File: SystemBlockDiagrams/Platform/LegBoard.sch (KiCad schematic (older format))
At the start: 12 parts

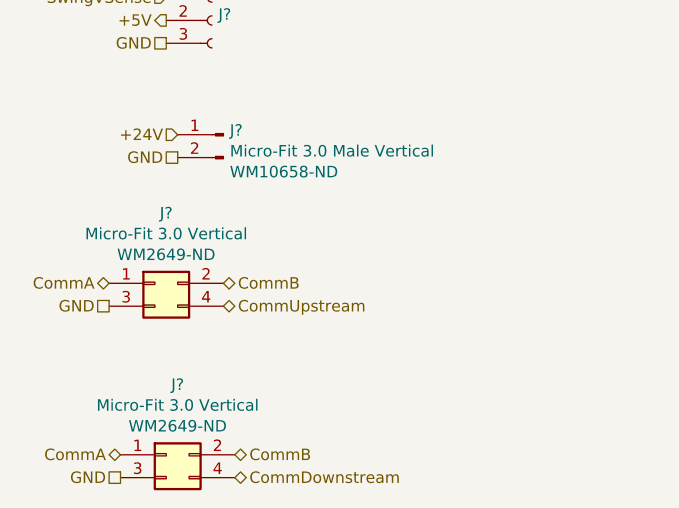
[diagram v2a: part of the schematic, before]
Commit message: Update to show all legs on block diagram
Add radios to platform diagram
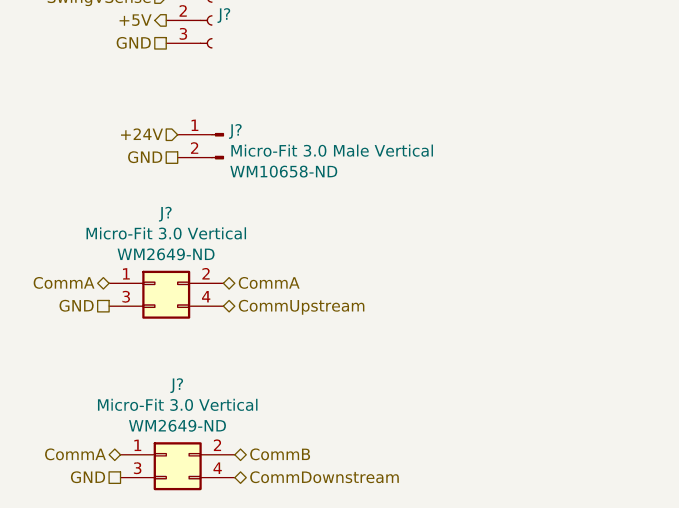
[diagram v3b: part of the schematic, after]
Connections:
- net CommA: now also J?.2 (Pin_2)
- net CommB: no longer J?.2 (Pin_2)
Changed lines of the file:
@@
 $Descr A4 11693 8268
 encoding utf-8
-Sheet 2 2
+Sheet 3 3
 Title ""
 Date ""
@@
 U 1 1 5E1D7814
 P 1250 1000
+AR Path="/5E1D533C/5E1D7814" Ref="J?"  Part="1"
+AR Path="/5E24C641/5E255C6B/5E1D7814" Ref="J?"  Part="1"
+AR Path="/5E264FF3/5E255C6B/5E1D7814" Ref="J?"  Part="1"
+AR Path="/5E2661DC/5E255C6B/5E1D7814" Ref="J?"  Part="1"
+AR Path="/5E269D38/5E255C6B/5E1D7814" Ref="J?"  Part="1"
+AR Path="/5E26B65F/5E255C6B/5E1D7814" Ref="J?"  Part="1"
+AR Path="/5E26CFEA/5E255C6B/5E1D7814" Ref="J?"  Part="1"
 F 0 "J?" H 1300 1407 50  0000 C CNN
 F 1 "Micro-Fit 3.0 Socket Vertical" H 1300 1316 50  0000 C CNN
@@
 U 1 1 5E1D7830
 P 1400 1600
+AR Path="/5E1D533C/5E1D7830" Ref="J?"  Part="1"
+AR Path="/5E24C641/5E255C6B/5E1D7830" Ref="J?"  Part="1"
+AR Path="/5E264FF3/5E255C6B/5E1D7830" Ref="J?"  Part="1"
+AR Path="/5E2661DC/5E255C6B/5E1D7830" Ref="J?"  Part="1"
+AR Path="/5E269D38/5E255C6B/5E1D7830" Ref="J?"  Part="1"
+AR Path="/5E26B65F/5E255C6B/5E1D7830" Ref="J?"  Part="1"
+AR Path="/5E26CFEA/5E255C6B/5E1D7830" Ref="J?"  Part="1"
 F 0 "J?" H 1428 1626 50  0000 L CNN
 F 1 "Micro-Fit 3.0 Vertical" H 1050 1850 50  0000 L CNN
@@
 U 1 1 5E1D7844
 P 1150 5300
+AR Path="/5E1D533C/5E1D7844" Ref="J?"  Part="1"
+AR Path="/5E24C641/5E255C6B/5E1D7844" Ref="J?"  Part="1"
+AR Path="/5E264FF3/5E255C6B/5E1D7844" Ref="J?"  Part="1"
+AR Path="/5E2661DC/5E255C6B/5E1D7844" Ref="J?"  Part="1"
+AR Path="/5E269D38/5E255C6B/5E1D7844" Ref="J?"  Part="1"
+AR Path="/5E26B65F/5E255C6B/5E1D7844" Ref="J?"  Part="1"
+AR Path="/5E26CFEA/5E255C6B/5E1D7844" Ref="J?"  Part="1"
 F 0 "J?" H 1200 5607 50  0000 C CNN
 F 1 "Micro-Fit 3.0 Vertical" H 1200 5516 50  0000 C CNN
@@
 U 1 1 5E2310FC
 P 1400 2900
+AR Path="/5E1D533C/5E2310FC" Ref="J?"  Part="1"
+AR Path="/5E24C641/5E255C6B/5E2310FC" Ref="J?"  Part="1"
+AR Path="/5E264FF3/5E255C6B/5E2310FC" Ref="J?"  Part="1"
+AR Path="/5E2661DC/5E255C6B/5E2310FC" Ref="J?"  Part="1"
+AR Path="/5E269D38/5E255C6B/5E2310FC" Ref="J?"  Part="1"
+AR Path="/5E26B65F/5E255C6B/5E2310FC" Ref="J?"  Part="1"
+AR Path="/5E26CFEA/5E255C6B/5E2310FC" Ref="J?"  Part="1"
 F 0 "J?" H 1428 2926 50  0000 L CNN
 F 1 "Micro-Fit 3.0 Vertical" H 1050 3150 50  0000 L CNN
@@
 U 1 1 5E232D29
 P 1400 4150
+AR Path="/5E1D533C/5E232D29" Ref="J?"  Part="1"
+AR Path="/5E24C641/5E255C6B/5E232D29" Ref="J?"  Part="1"
+AR Path="/5E264FF3/5E255C6B/5E232D29" Ref="J?"  Part="1"
+AR Path="/5E2661DC/5E255C6B/5E232D29" Ref="J?"  Part="1"
+AR Path="/5E269D38/5E255C6B/5E232D29" Ref="J?"  Part="1"
+AR Path="/5E26B65F/5E255C6B/5E232D29" Ref="J?"  Part="1"
+AR Path="/5E26CFEA/5E255C6B/5E232D29" Ref="J?"  Part="1"
 F 0 "J?" H 1428 4176 50  0000 L CNN
 F 1 "Micro-Fit 3.0 Vertical" H 1050 4400 50  0000 L CNN
@@
 U 1 1 5E238EBB
 P 1450 4650
+AR Path="/5E1D533C/5E238EBB" Ref="J?"  Part="1"
+AR Path="/5E24C641/5E255C6B/5E238EBB" Ref="J?"  Part="1"
+AR Path="/5E264FF3/5E255C6B/5E238EBB" Ref="J?"  Part="1"
+AR Path="/5E2661DC/5E255C6B/5E238EBB" Ref="J?"  Part="1"
+AR Path="/5E269D38/5E255C6B/5E238EBB" Ref="J?"  Part="1"
+AR Path="/5E26B65F/5E255C6B/5E238EBB" Ref="J?"  Part="1"
+AR Path="/5E26CFEA/5E255C6B/5E238EBB" Ref="J?"  Part="1"
 F 0 "J?" H 1422 4669 50  0000 R CNN
 F 1 "Micro-Fit 3.0 Male Vertical" H 1422 4578 50  0000 R CNN
@@
 CommA
 Text HLabel 1450 5300 2    50   BiDi ~ 0
-CommB
+CommA
 Text HLabel 1500 6050 2    50   BiDi ~ 0
 CommB
@@
 U 1 1 5E245915
 P 3100 1250
+AR Path="/5E1D533C/5E245915" Ref="D?"  Part="1"
+AR Path="/5E24C641/5E255C6B/5E245915" Ref="D?"  Part="1"
+AR Path="/5E264FF3/5E255C6B/5E245915" Ref="D?"  Part="1"
+AR Path="/5E2661DC/5E255C6B/5E245915" Ref="D?"  Part="1"
+AR Path="/5E269D38/5E255C6B/5E245915" Ref="D?"  Part="1"
+AR Path="/5E26B65F/5E255C6B/5E245915" Ref="D?"  Part="1"
+AR Path="/5E26CFEA/5E255C6B/5E245915" Ref="D?"  Part="1"
 F 0 "D?" H 3100 1747 50  0000 C CNN
 F 1 "LED_ABRG" H 3100 1656 50  0000 C CNN
@@
 U 1 1 5E246353
 P 3100 2200
+AR Path="/5E1D533C/5E246353" Ref="D?"  Part="1"
+AR Path="/5E24C641/5E255C6B/5E246353" Ref="D?"  Part="1"
+AR Path="/5E264FF3/5E255C6B/5E246353" Ref="D?"  Part="1"
+AR Path="/5E2661DC/5E255C6B/5E246353" Ref="D?"  Part="1"
+AR Path="/5E269D38/5E255C6B/5E246353" Ref="D?"  Part="1"
+AR Path="/5E26B65F/5E255C6B/5E246353" Ref="D?"  Part="1"
+AR Path="/5E26CFEA/5E255C6B/5E246353" Ref="D?"  Part="1"
 F 0 "D?" H 3100 2697 50  0000 C CNN
 F 1 "LED_ABRG" H 3100 2606 50  0000 C CNN
@@
 U 1 1 5E246805
 P 3100 3150
+AR Path="/5E1D533C/5E246805" Ref="D?"  Part="1"
+AR Path="/5E24C641/5E255C6B/5E246805" Ref="D?"  Part="1"
+AR Path="/5E264FF3/5E255C6B/5E246805" Ref="D?"  Part="1"
+AR Path="/5E2661DC/5E255C6B/5E246805" Ref="D?"  Part="1"
+AR Path="/5E269D38/5E255C6B/5E246805" Ref="D?"  Part="1"
+AR Path="/5E26B65F/5E255C6B/5E246805" Ref="D?"  Part="1"
+AR Path="/5E26CFEA/5E255C6B/5E246805" Ref="D?"  Part="1"
 F 0 "D?" H 3100 3647 50  0000 C CNN
 F 1 "LED_ABRG" H 3100 3556 50  0000 C CNN
@@
 U 1 1 5E23B759
 P 1250 2300
+AR Path="/5E1D533C/5E23B759" Ref="J?"  Part="1"
+AR Path="/5E24C641/5E255C6B/5E23B759" Ref="J?"  Part="1"
+AR Path="/5E264FF3/5E255C6B/5E23B759" Ref="J?"  Part="1"
+AR Path="/5E2661DC/5E255C6B/5E23B759" Ref="J?"  Part="1"
+AR Path="/5E269D38/5E255C6B/5E23B759" Ref="J?"  Part="1"
+AR Path="/5E26B65F/5E255C6B/5E23B759" Ref="J?"  Part="1"
+AR Path="/5E26CFEA/5E255C6B/5E23B759" Ref="J?"  Part="1"
 F 0 "J?" H 1300 2707 50  0000 C CNN
 F 1 "Micro-Fit 3.0 Socket Vertical" H 1300 2616 50  0000 C CNN
@@
 U 1 1 5E23C88B
 P 1250 3550
+AR Path="/5E1D533C/5E23C88B" Ref="J?"  Part="1"
+AR Path="/5E24C641/5E255C6B/5E23C88B" Ref="J?"  Part="1"
+AR Path="/5E264FF3/5E255C6B/5E23C88B" Ref="J?"  Part="1"
+AR Path="/5E2661DC/5E255C6B/5E23C88B" Ref="J?"  Part="1"
+AR Path="/5E269D38/5E255C6B/5E23C88B" Ref="J?"  Part="1"
+AR Path="/5E26B65F/5E255C6B/5E23C88B" Ref="J?"  Part="1"
+AR Path="/5E26CFEA/5E255C6B/5E23C88B" Ref="J?"  Part="1"
 F 0 "J?" H 1300 3957 50  0000 C CNN
 F 1 "Micro-Fit 3.0 Socket Vertical" H 1300 3866 50  0000 C CNN
@@
 U 1 1 5E2412AD
 P 1200 6050
+AR Path="/5E1D533C/5E2412AD" Ref="J?"  Part="1"
+AR Path="/5E24C641/5E255C6B/5E2412AD" Ref="J?"  Part="1"
+AR Path="/5E264FF3/5E255C6B/5E2412AD" Ref="J?"  Part="1"
+AR Path="/5E2661DC/5E255C6B/5E2412AD" Ref="J?"  Part="1"
+AR Path="/5E269D38/5E255C6B/5E2412AD" Ref="J?"  Part="1"
+AR Path="/5E26B65F/5E255C6B/5E2412AD" Ref="J?"  Part="1"
+AR Path="/5E26CFEA/5E255C6B/5E2412AD" Ref="J?"  Part="1"
 F 0 "J?" H 1250 6357 50  0000 C CNN
 F 1 "Micro-Fit 3.0 Vertical" H 1250 6266 50  0000 C CNN

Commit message: Added Digikey part numbers for 3-pin
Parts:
- J?: Manufacturer part Number 43650-0319 -> 43650-0316; Supplier Mouser -> Digikey; Supplier Part Number 538-43650-0319 -> WM1923-ND
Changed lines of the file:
@@
 EESchema Schematic File Version 4
-EELAYER 30 0
+EELAYER 26 0
 EELAYER END
 $Descr A4 11693 8268
 encoding utf-8
-Sheet 3 15
+Sheet 1 1
 Title ""
 Date ""
@@
 AR Path="/5E26B65F/5E255C6B/5E1D7814" Ref="J?"  Part="1"
 AR Path="/5E26CFEA/5E255C6B/5E1D7814" Ref="J?"  Part="1"
+AR Path="/5E1D7814" Ref="J?"  Part="1"
 F 0 "J?" H 1300 1407 50  0000 C CNN
 F 1 "Micro-Fit 3.0 Socket Vertical" H 1300 1316 50  0000 C CNN
@@
 AR Path="/5E26B65F/5E255C6B/5E1D7830" Ref="J?"  Part="1"
 AR Path="/5E26CFEA/5E255C6B/5E1D7830" Ref="J?"  Part="1"
+AR Path="/5E1D7830" Ref="J?"  Part="1"
 F 0 "J?" H 1428 1626 50  0000 L CNN
 F 1 "Micro-Fit 3.0 Vertical" H 1050 1850 50  0000 L CNN
 F 2 "" H 1400 1600 50  0001 C CNN
 F 3 "~" H 1400 1600 50  0001 C CNN
-F 4 "Mouser" H 1400 1600 50  0001 C CNN "Supplier"
-F 5 "538-43650-0319" H 1400 1600 50  0001 C CNN "Supplier Part Number"
+F 4 "Digikey" H 1400 1600 50  0001 C CNN "Supplier"
+F 5 "WM1923-ND" H 1400 1600 50  0001 C CNN "Supplier Part Number"
 F 6 "Molex" H 1400 1600 50  0001 C CNN "Manufacturer"
-F 7 "43650-0319" H 1400 1600 50  0001 C CNN "Manufacturer part Number"
+F 7 "43650-0316" H 1400 1600 50  0001 C CNN "Manufacturer part Number"
 	1    1400 1600
 	1    0    0    -1

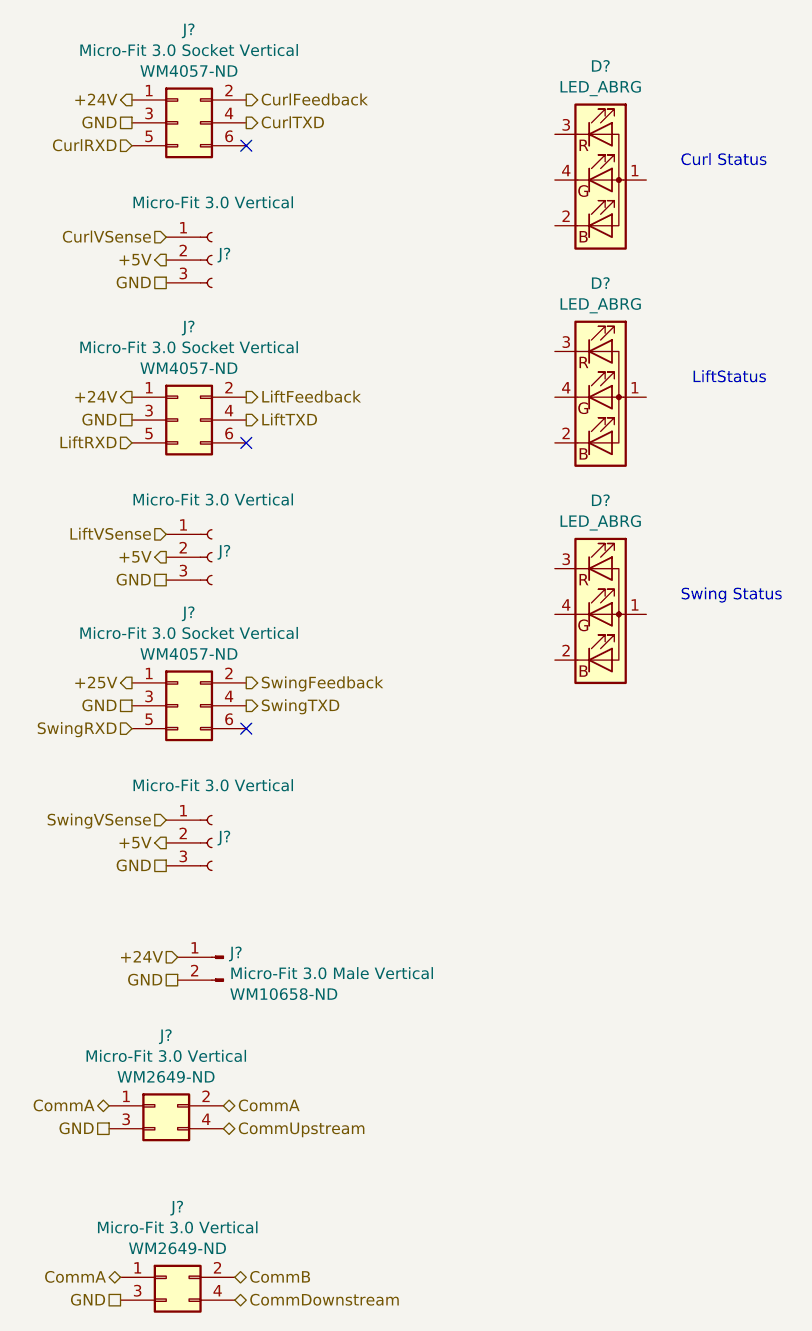
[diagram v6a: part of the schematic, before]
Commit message: Update part numbers for BOM generation
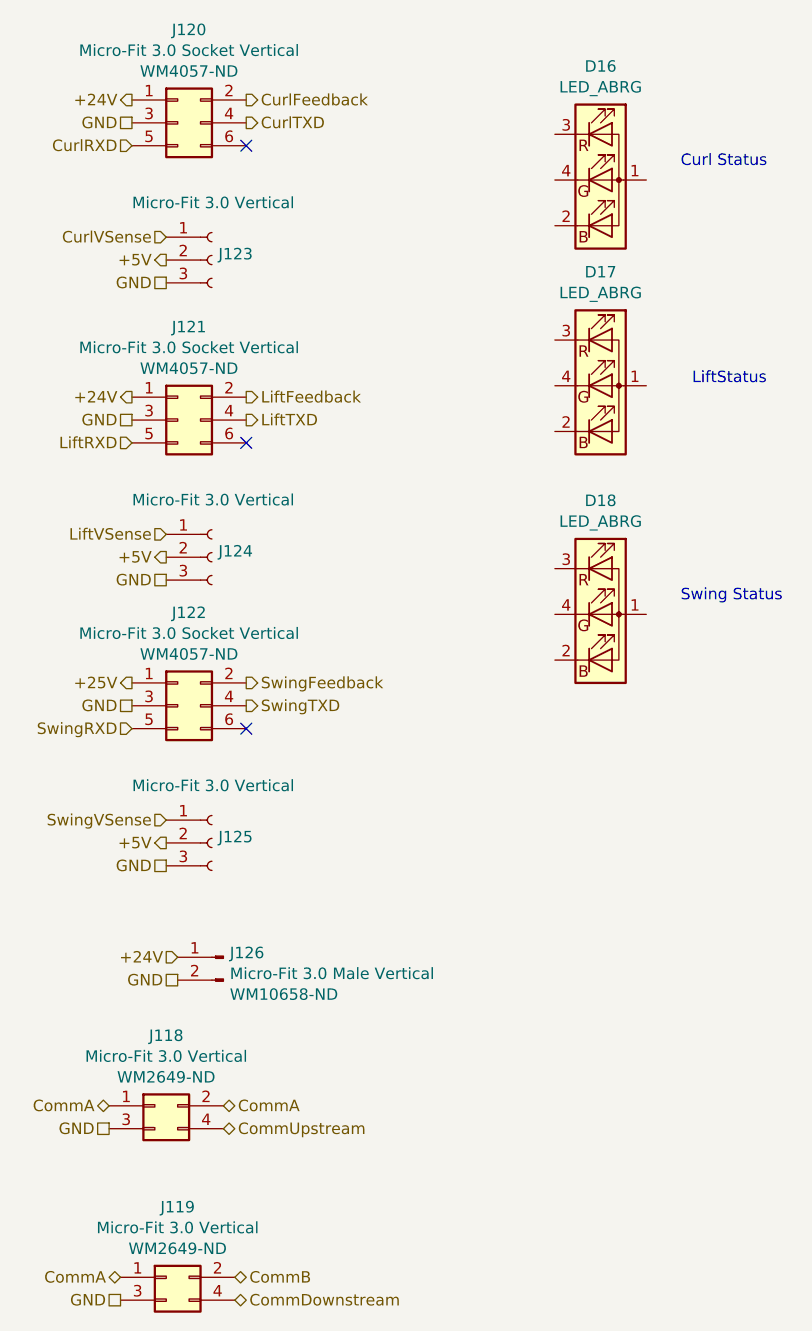
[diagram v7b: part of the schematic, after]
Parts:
- removed D? (x2): LED_ABRG, symbol Device:LED_ABRG
- added D2, D3: LED_ABRG, symbol Device:LED_ABRG
- D1: renamed from D?; Manufacturer (none) -> Würth Elektronik; Manufacturer Part Number (none) -> 150080M153000; Supplier (none) -> Digi-Key; Supplier Part Number (none) -> 732-11392-1-ND
- J33: renamed from J?; Manufacturer Part Number (none) -> 43650-0316; Manufacturer part Number 43650-0316 -> (none)
- J34, J35: renamed from J?; Manufacturer Part Number (none) -> 43650-0319; Manufacturer part Number 43650-0319 -> (none)
- gave numbers to parts that had none: 6
